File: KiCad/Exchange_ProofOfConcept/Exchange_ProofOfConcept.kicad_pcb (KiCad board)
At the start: 2 copper layers, 130.1 x 74.9 mm, 65 parts, among them J1 Conn_02x03_Odd_Even, J2 Conn_02x03_Odd_Even, J3 Conn_01x04, J7 Screw_Terminal_01x02, J9 Screw_Terminal_01x08, U1 MCP23017, U2 MCP23017, U3 MT8816

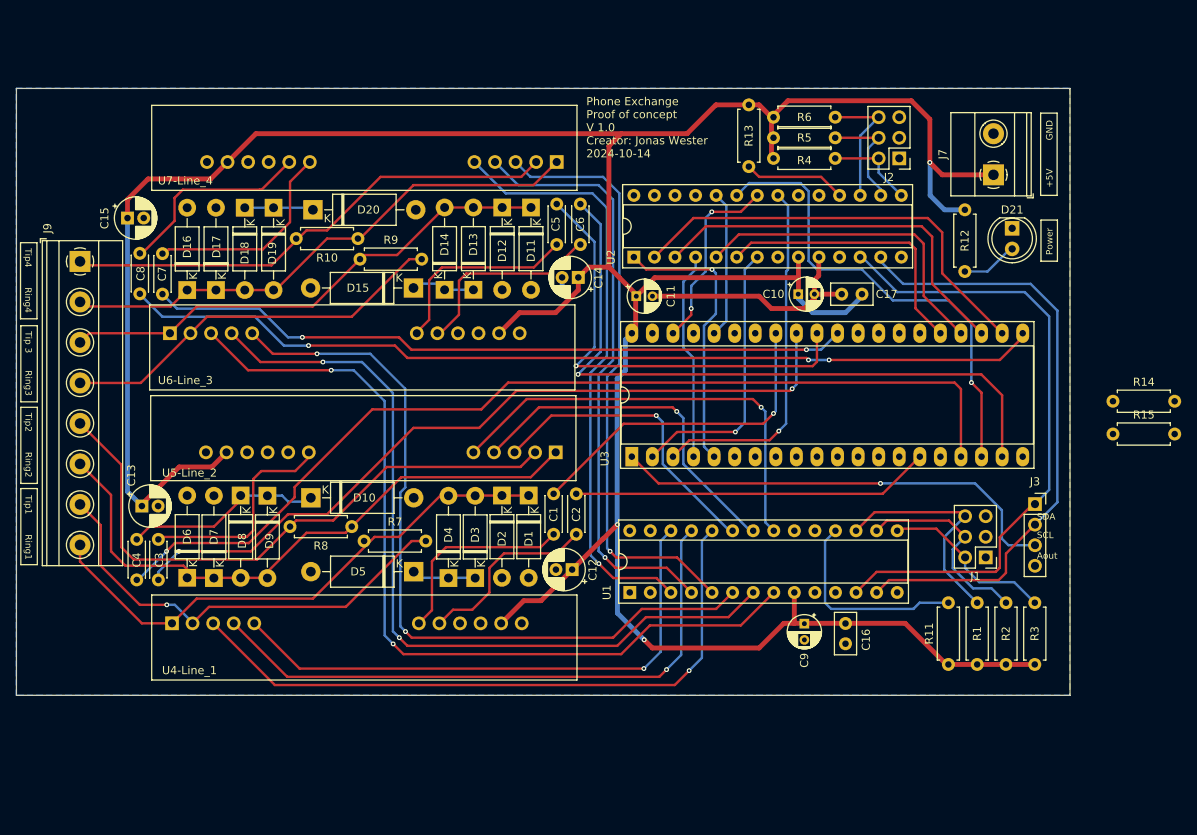
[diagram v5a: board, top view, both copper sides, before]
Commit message: deleted:    KiCad/Exchange_ProofOfConcept/Exchange_ProofOfConcept-backups/Exchange_ProofOfConcept-2024-09-22_005800.zip 	deleted:    KiCad/Exchange_ProofOfConcept/Exchange_ProofOfConcept-backups/Exchange_ProofOfConcept-2024-09-22_010415.zip 	deleted:    KiCad/Exchange_ProofOfConcept/Exchange_ProofOfConcept-backups/Exchange_ProofOfConcept-2024-09-22_093037.zip 	deleted:    KiCad/Exchange_ProofOfConcept/Exchange_ProofOfConcept-backups/Exchange_ProofOfConcept-2024-09-22_093847.zip 	deleted:    KiCad/Exchange_ProofOfConcept/Exchange_ProofOfConcept-backups/Exchange_ProofOfConcept-2024-09-22_094927.zip 	deleted:    KiCad/Exchange_ProofOfConcept/Exchange_ProofOfConcept-backups/Exchange_ProofOfConcept-2024-10-02_184119.zip 	deleted:    KiCad/Exchange_ProofOfConcept/Exchange_ProofOfConcept-backups/Exchange_ProofOfConcept-2024-10-06_223658.zip 	new file:   KiCad/Exchange_ProofOfConcept/Exchange_ProofOfConcept-backups/Exchange_ProofOfConcept-2024-11-20_223020.zip 	new file:   KiCad/Exchange_ProofOfConcept/Exchange_ProofOfConcept-backups/Exchange_ProofOfConcept-2024-11-20_223933.zip 	new file:   KiCad/Exchange_ProofOfConcept/Exchange_ProofOfConcept-backups/Exchange_ProofOfConcept-2024-11-20_224852.zip 	new file:   KiCad/Exchange_ProofOfConcept/Exchange_ProofOfConcept-backups/Exchange_ProofOfConcept-2024-11-20_230009.zip 	new file:   KiCad/Exchange_ProofOfConcept/Exchange_ProofOfConcept-backups/Exchange_ProofOfConcept-2024-11-20_231023.zip 	new file:   KiCad/Exchange_ProofOfConcept/Exchange_ProofOfConcept-backups/Exchange_ProofOfConcept-2024-11-20_231736.zip 	modified:   KiCad/Exchange_ProofOfConcept/Exchange_ProofOfConcept.kicad_pcb 	modified:   KiCad/Exchange_ProofOfConcept/Exchange_ProofOfConcept.kicad_prl 	modified:   KiCad/Exchange_ProofOfConcept/Exchange_ProofOfConcept.kicad_pro 	modified:   KiCad/Exchange_ProofOfConcept/Exchange_ProofOfConcept.kicad_sch 	modified:   KiCad/Exchange_ProofOfConcept/SLIC 1.kicad_sch 	modified:   KiCad/Exchange_ProofOfConcept/SLIC 1_sch.kicad_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
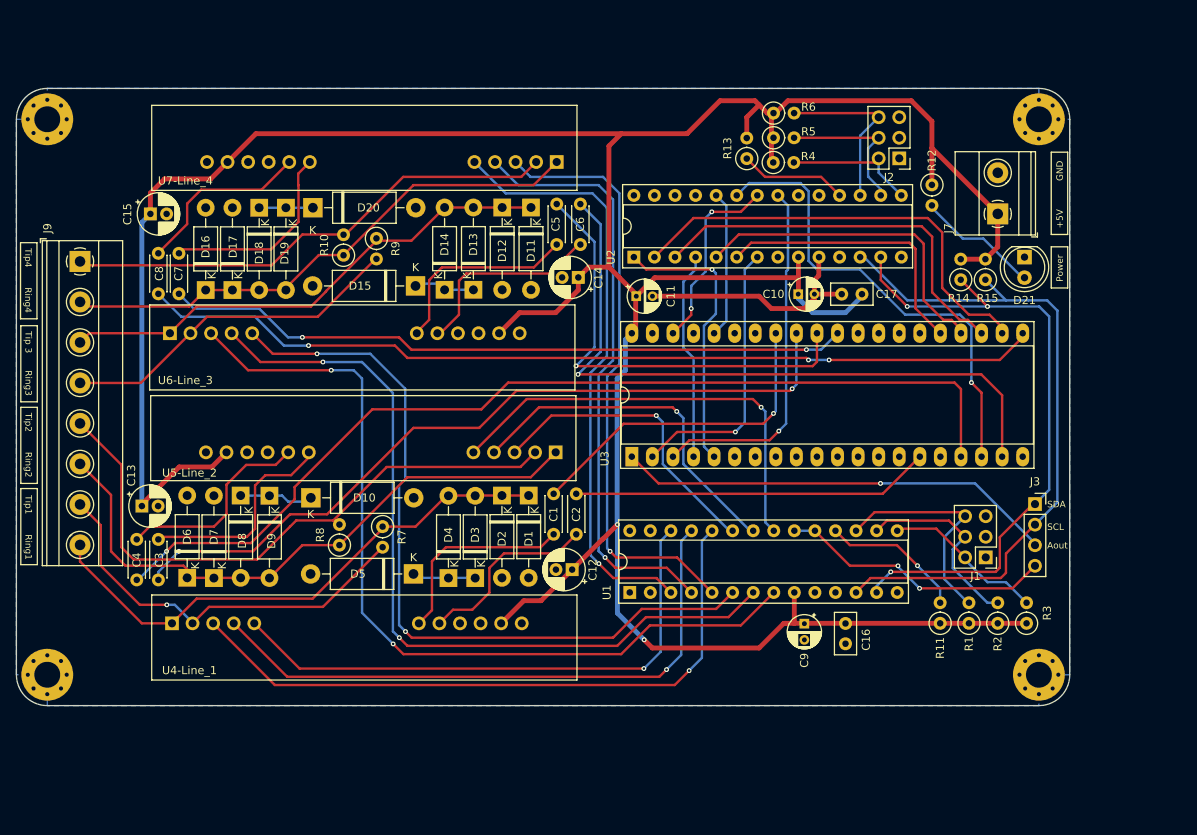
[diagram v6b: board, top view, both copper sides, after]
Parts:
- added H1: MountingHole_Pad, MountingHole:MountingHole_3.2mm_M3_Pad_Via, F.Cu at (80.0, 54.6)
- added H2: MountingHole_Pad, MountingHole:MountingHole_3.2mm_M3_Pad_Via, F.Cu at (202.4, 123.2)
- added H2: MountingHole_Pad, MountingHole:MountingHole_3.2mm_M3_Pad_Via, F.Cu at (202.4, 54.6)
- added H4: MountingHole_Pad, MountingHole:MountingHole_3.2mm_M3_Pad_Via, F.Cu at (80.0, 123.2)
- R1, R10, R11, R12, R13, R14, R15, R2, R3, R4, R5, R6, R7, R8, R9: footprint Resistor_THT:R_Axial_DIN0207_L6.3mm_D2.5mm_P7.62mm_Horizontal -> Resistor_THT:R_Axial_DIN0207_L6.3mm_D2.5mm_P2.54mm_Vertical
- moved R15 24.7 mm to (195.8, 74.4), turned to 90 degrees
- moved R14 24.0 mm to (192.8, 74.4), turned to 90 degrees
- moved R1 5.18 mm to (193.8, 116.8)
- moved R3 5.18 mm to (200.9, 116.8)
- moved R11 5.18 mm to (190.2, 116.8)
- moved R2 5.18 mm to (197.4, 116.8)
- moved R12 5.10 mm to (189.2, 62.7)
- moved J7 4.85 mm to (197.4, 66.3)
- moved D21 3.87 mm to (200.7, 71.6)
- moved R9 3.28 mm to (120.7, 69.3), turned to -90 degrees
- moved R7 2.90 mm to (121.4, 104.9), turned to -90 degrees
- moved C15 2.87 mm to (92.7, 66.3)
- moved R8 2.75 mm to (116.1, 107.2), turned to 90 degrees
- moved R10 2.72 mm to (116.6, 71.4), turned to 90 degrees
- moved C8 2.29 mm to (93.7, 71.2)
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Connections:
- R14 pad 2: unconnected-(R14-Pad2) -> /5V
- R15 pad 2: unconnected-(R15-Pad2) -> /5V
- U1 pad 12: /SDA -> /SCL
- U1 pad 13: /SCL -> /SDA
- U2 pad 12: /SDA -> /SCL
- U2 pad 13: /SCL -> /SDA
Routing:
- net /SLIC INT: track 0.00 -> 33.9 mm, vias 0 -> 2
- net Net-(U5-Line_2-Audio_out): track 16.1 -> 25.3 mm
- net /SCL: track 76.8 -> 85.5 mm
- net Net-(D21-A): track 6.75 -> 15.3 mm
- net Net-(U1-~{RESET}): track 25.3 -> 17.6 mm, vias 0 -> 1
- net /5V: track 382.1 -> 387.8 mm, vias 3 -> 2
- net /TIP_1: track 56.0 -> 50.3 mm
- net Net-(J2-Pin_6): track 16.2 -> 21.8 mm
- net /RING_3: track 48.5 -> 43.2 mm
- net Net-(J2-Pin_2): track 11.9 -> 16.9 mm
- net Net-(J2-Pin_4): track 13.9 -> 18.7 mm
- net Net-(U7-Line_4-Audio_out): track 24.8 -> 22.3 mm
- net /Aout_4: track 114.1 -> 111.7 mm
- net /SDA: track 79.1 -> 81.3 mm, vias 0 -> 3
- net /Ain_4: track 87.0 -> 85.0 mm
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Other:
- board size 130.1 x 74.9 mm -> 130 x 76.2 mm
- board text added: "Phone Exchange Proof of concept V 2.0 Creator: Jonas Wester 2024-11-20"
- board text removed: "Phone Exchange Proof of concept V 1.0 Creator: Jonas Wester 2024-10-14"

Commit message: new file:   KiCad/Exchange_ProofOfConcept/#auto_saved_files# 	deleted:    KiCad/Exchange_ProofOfConcept/Exchange_ProofOfConcept-backups/Exchange_ProofOfConcept-2024-10-10_194257.zip 	deleted:    KiCad/Exchange_ProofOfConcept/Exchange_ProofOfConcept-backups/Exchange_ProofOfConcept-2024-11-20_223020.zip 	new file:   KiCad/Exchange_ProofOfConcept/Exchange_ProofOfConcept-backups/Exchange_ProofOfConcept-2024-11-26_195718.zip 	new file:   KiCad/Exchange_ProofOfConcept/Exchange_ProofOfConcept-backups/Exchange_ProofOfConcept-2024-11-26_201040.zip 	new file:   KiCad/Exchange_ProofOfConcept/Exchange_ProofOfConcept-backups/Exchange_ProofOfConcept-2024-11-26_201745.zip 	modified:   KiCad/Exchange_ProofOfConcept/Exchange_ProofOfConcept.kicad_pcb 	modified:   KiCad/Exchange_ProofOfConcept/Exchange_ProofOfConcept.kicad_pro 	modified:   KiCad/Exchange_ProofOfConcept/Exchange_ProofOfConcept.kicad_sch 	new file:   KiCad/Exchange_ProofOfConcept/Exchange_ProofOfConcept.pdf 	new file:   KiCad/Exchange_ProofOfConcept/_autosave-Exchange_ProofOfConcept.kicad_sch 	new file:   KiCad/Exchange_ProofOfConcept/~Exchange_ProofOfConcept.kicad_pcb.lck 	new file:   KiCad/Exchange_ProofOfConcept/~Exchange_ProofOfConcept.kicad_sch.lck 	new file:   docs/Exchange_ProofOfConcept.pdf
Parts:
- removed the H2 at (202.4, 123.2)
- removed the H2 at (202.4, 54.6)
- added H2: MountingHole_Pad, MountingHole:MountingHole_3.2mm_M3_Pad_Via, F.Cu at (202.4, 54.6)
- added H3: MountingHole_Pad, MountingHole:MountingHole_3.2mm_M3_Pad_Via, F.Cu at (202.4, 123.3)
- J3: value Conn_01x04 -> Conn_01x05; footprint Connector_PinSocket_2.54mm:PinSocket_1x04_P2.54mm_Vertical -> Connector_PinHeader_2.54mm:PinHeader_1x05_P2.54mm_Vertical
- moved J3 1.65 mm to (200.9, 100.8)
- moved R13 0.48 mm to (166.4, 59.9), turned to 180 degrees
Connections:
- R11 pad 1: /5V -> /MCP_reset
- R13 pad 2: /5V -> /MCP_reset
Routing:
- net /MCP_reset: track 0.00 -> 95.9 mm, vias 0 -> 3
- net /5V: track 387.8 -> 384.5 mm
- net Net-(U2-GPB6): track 34.2 -> 36.5 mm
- net Net-(U2-GPA1): track 23.4 -> 25.4 mm
- net /Aout_x: track 54.4 -> 52.7 mm
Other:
- board text added: "Int"
- board text added: "MCP Reset"

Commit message: Changes to be committed: 	new file:   KiCad/Exchange_ProofOfConcept/ESP-Unit/ESP-Unit-backups/ESP-Unit-2024-11-30_004013.zip 	new file:   KiCad/Exchange_ProofOfConcept/ESP-Unit/ESP-Unit-backups/ESP-Unit-2024-11-30_005151.zip 	new file:   KiCad/Exchange_ProofOfConcept/ESP-Unit/ESP-Unit-backups/ESP-Unit-2024-11-30_173159.zip 	new file:   KiCad/Exchange_ProofOfConcept/ESP-Unit/ESP-Unit-backups/ESP-Unit-2024-12-02_225320.zip 	new file:   KiCad/Exchange_ProofOfConcept/ESP-Unit/ESP-Unit-backups/ESP-Unit-2024-12-02_230401.zip 	new file:   KiCad/Exchange_ProofOfConcept/ESP-Unit/ESP-Unit-backups/ESP-Unit-2024-12-02_231401.zip 	new file:   KiCad/Exchange_ProofOfConcept/ESP-Unit/ESP-Unit-backups/ESP-Unit-2024-12-02_232414.zip 	new file:   KiCad/Exchange_ProofOfConcept/ESP-Unit/ESP-Unit-backups/ESP-Unit-2024-12-02_233354.zip 	new file:   KiCad/Exchange_ProofOfConcept/ESP-Unit/ESP-Unit-backups/ESP-Unit-2024-12-04_223019.zip 	new file:   KiCad/Exchange_ProofOfConcept/ESP-Unit/ESP-Unit-backups/ESP-Unit-2024-12-04_223655.zip 	new file:   KiCad/Exchange_ProofOfConcept/ESP-Unit/ESP-Unit-backups/ESP-Unit-2024-12-04_225021.zip 	new file:   KiCad/Exchange_ProofOfConcept/ESP-Unit/ESP-Unit-backups/ESP-Unit-2024-12-04_230524.zip 	new file:   KiCad/Exchange_ProofOfConcept/ESP-Unit/ESP-Unit-backups/ESP-Unit-2024-12-04_231506.zip 	new file:   KiCad/Exchange_ProofOfConcept/ESP-Unit/ESP-Unit-backups/ESP-Unit-2024-12-05_032122.zip 	new file:   KiCad/Exchange_ProofOfConcept/ESP-Unit/ESP-Unit-backups/ESP-Unit-2024-12-06_183750.zip 	new file:   KiCad/Exchange_ProofOfConcept/ESP-Unit/ESP-Unit-backups/ESP-Unit-2024-12-07_112304.zip 	new file:   KiCad/Exchange_ProofOfConcept/ESP-Unit/ESP-Unit-backups/ESP-Unit-2024-12-07_125326.zip 	modified:   KiCad/Exchange_ProofOfConcept/ESP-Unit/ESP-Unit.kicad_pcb 	modified:   KiCad/Exchange_ProofOfConcept/ESP-Unit/ESP-Unit.kicad_prl 	modified:   KiCad/Exchange_ProofOfConcept/ESP-Unit/ESP-Unit.kicad_pro 	modified:   KiCad/Exchange_ProofOfConcept/ESP-Unit/ESP-Unit.k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
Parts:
- J3: value Conn_01x05 -> Conn_01x07; footprint Connector_PinHeader_2.54mm:PinHeader_1x05_P2.54mm_Vertical -> Connector_PinSocket_2.54mm:PinSocket_1x07_P2.54mm_Vertical
- moved R11 6.14 mm to (184.7, 119.4)
- moved R1 6.14 mm to (188.2, 119.4)
- moved R2 6.14 mm to (191.8, 119.4)
- moved R3 6.14 mm to (195.3, 119.4)
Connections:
- J3 pad 3: /Aout_x -> /SLIC_INT
- J3 pad 4: /SLIC INT -> /MCP_reset
- J3 pad 5: /MCP_reset -> /Aout_x
- U1 pad 19: /SLIC INT -> /SLIC_INT
- U1 pad 20: /SLIC INT -> /SLIC_INT
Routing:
- net /SLIC_INT: track 0.00 -> 35.7 mm, vias 0 -> 2
- net /SLIC INT: track 33.4 -> 0.00 mm, vias 2 -> 0
- net /Aout_x: track 52.7 -> 58.6 mm
- net /5V: track 384.5 -> 389.4 mm
- net /MCP_reset: track 95.9 -> 99.8 mm
- net Net-(U1-~{RESET}): track 17.6 -> 20.8 mm
- net Net-(J1-Pin_6): track 27.7 -> 30.0 mm
- net Net-(J1-Pin_2): track 20.0 -> 18.9 mm
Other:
- board text added: "5V"
